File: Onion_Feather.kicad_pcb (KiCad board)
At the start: 4 copper layers, 59.7 x 53.3 mm, 71 parts, among them IC1 MAX11646EUA+T, IC2 SN74HC367PWR, J1 HR911105A, J2 CON_HEADER_PRG_AVR_ICSP-PTH, J3 Conn_01x02, J4 USB_A, J5 M04PTH, U1 ONION-OMEGA2, U2 AP1117-33, U3 CP2102N-A01-GQFN24, U4 BQ25895RTW, U5 STF202-22T1G

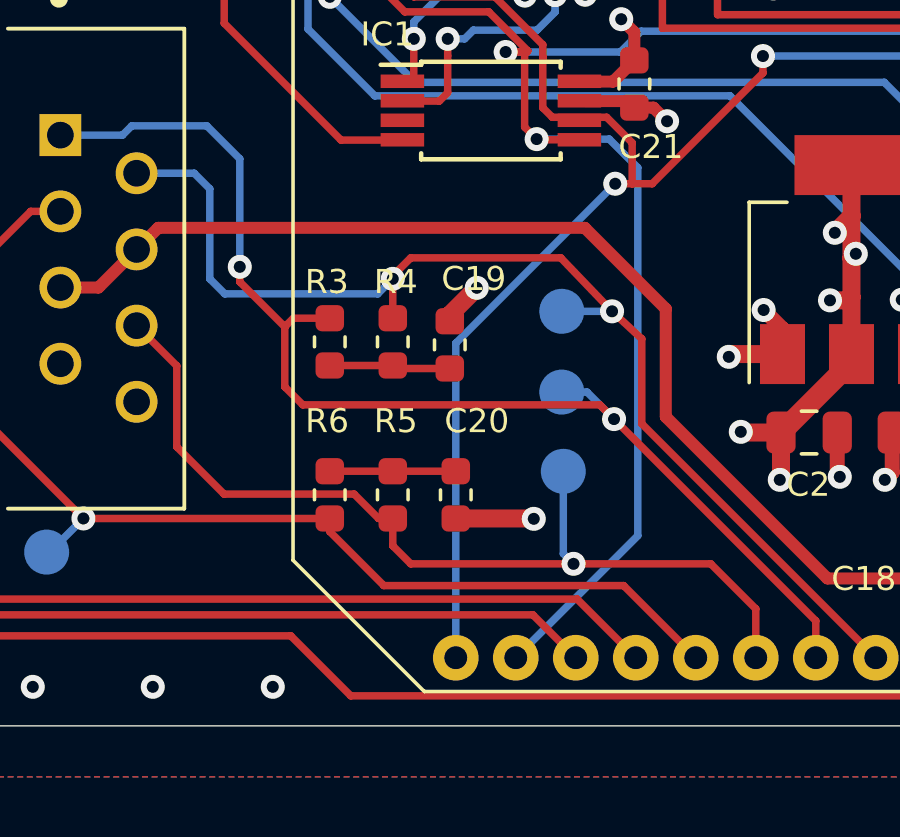
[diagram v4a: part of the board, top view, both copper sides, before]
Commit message: #9 Tie center pin to NET_POW
Signed-off-by: Tisham Dhar <whatnickd@gmail.com>
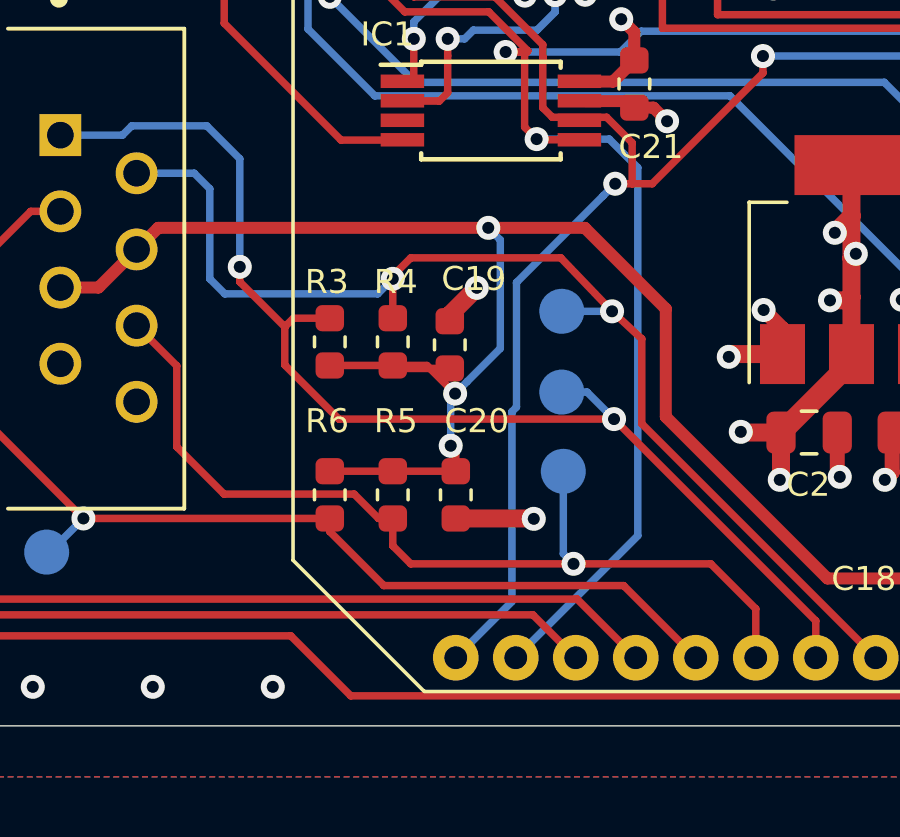
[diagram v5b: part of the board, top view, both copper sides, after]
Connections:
- C19 pad 1: Net-(C19-Pad1) -> NET_POW
- C20 pad 1: Net-(C20-Pad1) -> NET_POW
- R3 pad 1: Net-(C19-Pad1) -> NET_POW
- R4 pad 1: Net-(C19-Pad1) -> NET_POW
- R5 pad 1: Net-(C20-Pad1) -> NET_POW
- R6 pad 1: Net-(C20-Pad1) -> NET_POW
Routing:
- net NET_POW: track 39.5 -> 59.3 mm, vias 0 -> 3
- net Net-(C20-Pad1): track 4.20 -> 0.00 mm
- net Net-(C19-Pad1): track 4.04 -> 0.00 mm

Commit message: New manufacture files
Signed-off-by: Tisham Dhar <whatnickd@gmail.com>
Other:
- board text added: "Onion-Omega to Feather Adapter v0.0.2 30/09/2020 by Tisham (whatnick) Dhar OSHW TAPR"
- board text removed: "Onion-Omega to Feather Adapter v0.0.1 20/04/2020 by Tisham (whatnick) Dhar OSHW TAPR"
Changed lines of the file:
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@@
   (general
     (thickness 1.6)
-    (drawings 18)
+    (drawings 19)
     (tracks 1148)
     (zones 0)
@@
       (net 52 "/Power Subsystems/ID"))
   )
-  (gr_text "Onion-Omega to Feather Adapter\nv0.0.1 20/04/2020\nby Tisham (whatnick) Dhar\nOSHW TAPR" (at 149.86 95.25) (layer B.SilkS)
+  (dimension 59.690012 (width 0.15) (layer Dwgs.User)
+    (gr_text "59.690 mm" (at 137.784445 128.31418 -0.03657176919) (layer Dwgs.User)
+      (effects (font (size 1 1) (thickness 0.15)))
+    )
+    (feature1 (pts (xy 107.95 111.76) (xy 107.939901 127.581551)))
+    (feature2 (pts (xy 167.64 111.7981) (xy 167.629901 127.619651)))
+    (crossbar (pts (xy 167.630275 127.03323) (xy 107.940275 126.99513)))
+    (arrow1a (pts (xy 107.940275 126.99513) (xy 109.067153 126.409428)))
+    (arrow1b (pts (xy 107.940275 126.99513) (xy 109.066404 127.58227)))
+    (arrow2a (pts (xy 167.630275 127.03323) (xy 166.504146 126.44609)))
+    (arrow2b (pts (xy 167.630275 127.03323) (xy 166.503397 127.618932)))
+  )
+  (gr_text "Onion-Omega to Feather Adapter\nv0.0.2 30/09/2020\nby Tisham (whatnick) Dhar\nOSHW TAPR" (at 149.86 95.25) (layer B.SilkS)
     (effects (font (size 1 1) (thickness 0.15)) (justify mirror))
   )

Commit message: Move to KiCAD nightly
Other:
- net class Default removed
